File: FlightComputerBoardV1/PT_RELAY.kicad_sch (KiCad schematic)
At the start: 4 parts, among them J1 Screw_Terminal_01x02, J2 Screw_Terminal_01x02, J3 Screw_Terminal_01x02, J4 Screw_Terminal_01x02

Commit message: Added PTs
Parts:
- added C1, C2, C3, C4, C5, C6: 0.1u, symbol Device:C
- added J5: PT5, symbol Connector:Screw_Terminal_01x02
- added J6: PT6, symbol Connector:Screw_Terminal_01x02
- added R1, R11, R3, R5, R7, R9: 1k, symbol Device:R_US
- added R10, R12, R2, R4, R6, R8: 160, symbol Device:R_US
- J1: value Screw_Terminal_01x02 -> PT1
- J2: value Screw_Terminal_01x02 -> PT2
- J3: value Screw_Terminal_01x02 -> PT3
- J4: value Screw_Terminal_01x02 -> PT4
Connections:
- net +24V: now reaches J3.1 (Pin_1)
- net +24V: now also J1.1 (Pin_1), J2.1 (Pin_1), J4.1 (Pin_1), J5.1 (Pin_1), J6.1 (Pin_1)
- net at J3.2 (Pin_2): now also R5.1
- net at J4.2 (Pin_2): now also R7.1
- net at J1.2 (Pin_2): now also R1.1
- net at J2.2 (Pin_2): now also R3.1
- new net: J5.2 (Pin_2), R9.1
- new net: J6.2 (Pin_2), R11.1
- new net GND: C1.2, C2.2, C3.2, C4.2, C5.2, C6.2, R10.2, R12.2, R2.2, R4.2, R6.2, R8.2
- new net PT1: C1.1, R1.2, R2.1
- new net PT2: C2.1, R3.2, R4.1
- new net PT3: C3.1, R5.2, R6.1
- new net PT4: C4.1, R7.2, R8.1
- new net PT5: C5.1, R10.1, R9.2
- new net PT6: C6.1, R11.2, R12.1
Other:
- moved on the sheet: J1

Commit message: Added 9 PTs circuit
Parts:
- added C7, C8, C9: 0.1u, symbol Device:C
- added J7: PT7, symbol Connector:Screw_Terminal_01x02
- added J8: PT8, symbol Connector:Screw_Terminal_01x02
- added J9: PT9, symbol Connector:Screw_Terminal_01x02
- added R13, R15, R17: 1k, symbol Device:R_US
- added R14, R16, R18: 160, symbol Device:R_US
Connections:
- net +24V: now also J7.1 (Pin_1), J8.1 (Pin_1), J9.1 (Pin_1)
- net GND: now also C7.2, C8.2, C9.2, R14.2, R16.2, R18.2
- new net: J9.2 (Pin_2), R17.1
- new net: J7.2 (Pin_2), R13.1
- new net: J8.2 (Pin_2), R15.1
- new net PT7: C7.1, R13.2, R14.1
- new net PT8: C8.1, R15.2, R16.1
- new net PT9: C9.1, R17.2, R18.1
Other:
- note added: "9x PRESSURE TRANSDUCERS"
- moved on the sheet: C1, C2, C3, C4, C5, C6, J1, J2, J3, J4, J5, J6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

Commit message: Added 6x relay-driven solenoids circuit
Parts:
- added D1, D2, D3, D4, D5, D6: 1N4007, Diode_THT:D_DO-41_SOD81_P10.16mm_Horizontal, symbol Diode:1N4007
- added J10: RELAY1, symbol Connector:Screw_Terminal_01x02
- added J11: RELAY4, symbol Connector:Screw_Terminal_01x02
- added J12: RELAY2, symbol Connector:Screw_Terminal_01x02
- added J13: RELAY5, symbol Connector:Screw_Terminal_01x02
- added J14: RELAY3, symbol Connector:Screw_Terminal_01x02
- added J15: RELAY6, symbol Connector:Screw_Terminal_01x02
- added Q1, Q2, Q3, Q4, Q5, Q6: Q_NPN, symbol Device:Q_NPN
- added R19, R24, R29, R30, R37, R38: 670, symbol Device:R_US
- added R20, R22, R23, R26, R27, R28, R33, R34, R35, R36, R41, R42: 10k, symbol Device:R_US
- added R21, R25, R31, R32, R39, R40: 4.7k, symbol Device:R_US
- added U1, U2, U3, U4, U5, U6: PS2811-1-F3-A, PS2811-1_REN, symbol PS2811_1_F3_A:PS2811-1-F3-A
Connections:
- net GND: now also R20.1, R23.1, R27.1, R28.1, R35.1, R36.1, U1.2 (CATHODE), U2.2 (CATHODE), U3.2 (CATHODE), U4.2 (CATHODE), U5.2 (CATHODE), U6.2 (CATHODE)
- new net: D1.2 (A), J10.2 (Pin_2), Q1.C
- new net: Q5.B, R39.2, R41.2
- new net: D5.2 (A), J14.2 (Pin_2), Q5.C
- new net: R31.1, U3.3 (EMITTER)
- new net: Q3.B, R31.2, R33.2
- new net: Q6.B, R40.2, R42.2
- new net: D4.2 (A), J13.2 (Pin_2), Q4.C
- new net: R38.2, U6.1 (ANODE)
- new net: R40.1, U6.3 (EMITTER)
- new net: Q4.B, R32.2, R34.2
- new net: D6.2 (A), J15.2 (Pin_2), Q6.C
- new net: R37.2, U5.1 (ANODE)
- new net: R24.2, U2.1 (ANODE)
- new net: R25.1, U2.3 (EMITTER)
- new net: Q1.B, R21.2, R22.2
- new net: R21.1, U1.3 (EMITTER)
- new net: D3.2 (A), J12.2 (Pin_2), Q3.C
- new net: R30.2, U4.1 (ANODE)
- new net: R39.1, U5.3 (EMITTER)
- new net: Q2.B, R25.2, R26.2
- new net: D2.2 (A), J11.2 (Pin_2), Q2.C
- new net: R19.2, U1.1 (ANODE)
- new net: R29.2, U3.1 (ANODE)
- new net: R32.1, U4.3 (EMITTER)
- new net HI_24V: D1.1 (K), D2.1 (K), D3.1 (K), D4.1 (K), D5.1 (K), D6.1 (K), J10.1 (Pin_1), J11.1 (Pin_1), J12.1 (Pin_1), J13.1 (Pin_1), J14.1 (Pin_1), J15.1 (Pin_1), U1.4 (COLLECTOR), U2.4 (COLLECTOR), U3.4 (COLLECTOR), U4.4 (COLLECTOR), U5.4 (COLLECTOR), U6.4 (COLLECTOR)
- new net HI_24_GND: Q1.E, Q2.E, Q3.E, Q4.E, Q5.E, Q6.E, R22.1, R26.1, R33.1, R34.1, R41.1, R42.1
- new net RELAY1: R19.1, R20.2
- new net RELAY2: R27.2, R29.1
- new net RELAY3: R35.2, R37.1
- new net RELAY4: R23.2, R24.1
- new net RELAY5: R28.2, R30.1
- new net RELAY6: R36.2, R38.1
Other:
- note added: "6x RELAY-DRIVEN SOLENOIDS"

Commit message: Added sheets and hierarchy labels
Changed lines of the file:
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@@
 		)
 	)
-	(global_label "PT7"
+	(hierarchical_label "PT3"
 		(shape output)
-		(at 281.94 50.8 180)
-		(fields_autoplaced yes)
+		(at 123.19 50.8 180)
 		(effects
 			(font
@@
 			(justify right)
 		)
-		(property "Intersheetrefs" "${INTERSHEET_REFS}"
-			(at 275.5077 50.8 0)
-			(hide yes)
-			(show_name no)
-			(do_not_autoplace no)
-			(effects
-				(font
-					(size 1.27 1.27)
-				)
-				(justify right)
-			)
-		)
 	)
-	(global_label "PT2"
+	(hierarchical_label "PT2"
 		(shape output)
 		(at 80.01 50.8 180)
-		(fields_autoplaced yes)
 		(effects
 			(font
@@
 			(justify right)
 		)
-		(property "Intersheetrefs" "${INTERSHEET_REFS}"
-			(at 73.5777 50.8 0)
-			(hide yes)
-			(show_name no)
-			(do_not_autoplace no)
-			(effects
-				(font
-					(size 1.27 1.27)
-				)
-				(justify right)
-			)
-		)
 	)
-	(global_label "PT1"
+	(hierarchical_label "PT6"
 		(shape output)
-		(at 36.83 50.8 180)
-		(fields_autoplaced yes)
+		(at 246.38 50.8 180)
 		(effects
 			(font
@@
 			(justify right)
 		)
-		(property "Intersheetrefs" "${INTERSHEET_REFS}"
-			(at 30.3977 50.8 0)
-			(hide yes)
-			(show_name no)
-			(do_not_autoplace no)
-			(effects
-				(font
-					(size 1.27 1.27)
-				)
-				(justify right)
-			)
-		)
 	)
-	(global_label "PT9"
+	(hierarchical_label "PT5"
 		(shape output)
-		(at 365.76 50.8 180)
-		(fields_autoplaced yes)
+		(at 208.28 50.8 180)
 		(effects
 			(font
@@
 			(justify right)
 		)
-		(property "Intersheetrefs" "${INTERSHEET_REFS}"
-			(at 359.3277 50.8 0)
-			(hide yes)
-			(show_name no)
-			(do_not_autoplace no)
-			(effects
-				(font
-					(size 1.27 1.27)
-				)
-				(justify right)
-			)
-		)
 	)
-	(global_label "PT8"
+	(hierarchical_label "PT1"
 		(shape output)
-		(at 322.58 50.8 180)
-		(fields_autoplaced yes)
+		(at 36.83 50.8 180)
 		(effects
 			(font
@@
 			(justify right)
 		)
-		(property "Intersheetrefs" "${INTERSHEET_REFS}"
-			(at 316.1477 50.8 0)
-			(hide yes)
-			(show_name no)
-			(do_not_autoplace no)
-			(effects
-				(font
-					(size 1.27 1.27)
-				)
-				(justify right)
-			)
-		)
 	)
-	(global_label "PT4"
+	(hierarchical_label "PT4"
 		(shape output)
 		(at 166.37 50.8 180)
-		(fields_autoplaced yes)
 		(effects
 			(font
@@
 			(justify right)
 		)
-		(property "Intersheetrefs" "${INTERSHEET_REFS}"
-			(at 159.9377 50.8 0)
-			(hide yes)
-			(show_name no)
-			(do_not_autoplace no)
-			(effects
-				(font
-					(size 1.27 1.27)
-				)
-				(justify right)
-			)
-		)
 	)
-	(global_label "PT5"
+	(hierarchical_label "PT7"
 		(shape output)
-		(at 208.28 50.8 180)
-		(fields_autoplaced yes)
+		(at 281.94 50.8 180)
 		(effects
 			(font
@@
 			(justify right)
 		)
-		(property "Intersheetrefs" "${INTERSHEET_REFS}"
-			(at 201.8477 50.8 0)
-			(hide yes)
-			(show_name no)
-			(do_not_autoplace no)
-			(effects
-				(font
-					(size 1.27 1.27)
-				)
-				(justify right)
-			)
-		)
 	)
-	(global_label "PT3"
+	(hierarchical_label "PT8"
 		(shape output)
-		(at 123.19 50.8 180)
-		(fields_autoplaced yes)
+		(at 322.58 50.8 180)
 		(effects
 			(font
@@
 			(justify right)
 		)
-		(property "Intersheetrefs" "${INTERSHEET_REFS}"
-			(at 116.7577 50.8 0)
-			(hide yes)
-			(show_name no)
-			(do_not_autoplace no)
-			(effects
-				(font
-					(size 1.27 1.27)
-				)
-				(justify right)
-			)
-		)
 	)
-	(global_label "PT6"
+	(hierarchical_label "PT9"
 		(shape output)
-		(at 246.38 50.8 180)
-		(fields_autoplaced yes)
+		(at 365.76 50.8 180)
 		(effects
 			(font
@@
 			(justify right)
 		)
-		(property "Intersheetrefs" "${INTERSHEET_REFS}"
-			(at 239.9477 50.8 0)
-			(hide yes)
-			(show_name no)
-			(do_not_autoplace no)
-			(effects
-				(font
-					(size 1.27 1.27)
-				)
-				(justify right)
-			)
-		)
 	)

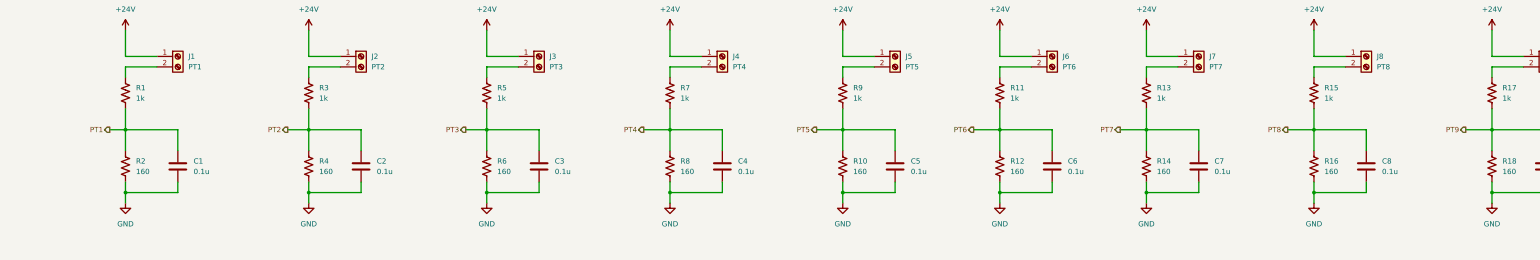
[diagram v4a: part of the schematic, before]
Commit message: Addition to MCU sheet and peripheral connection complete
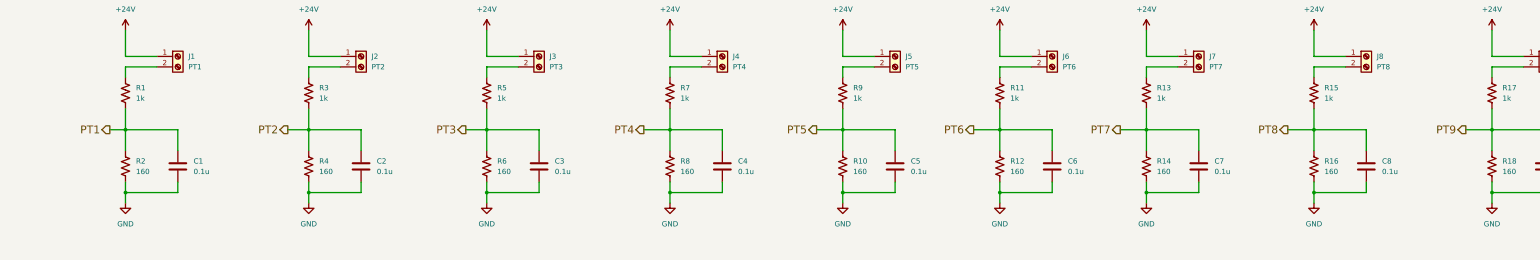
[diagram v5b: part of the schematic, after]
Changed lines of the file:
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@@
 		(effects
 			(font
-				(size 1.27 1.27)
+				(size 1.905 1.905)
 			)
 			(justify right)
@@
 		(effects
 			(font
-				(size 1.27 1.27)
+				(size 1.905 1.905)
 			)
 			(justify right)
@@
 		(effects
 			(font
-				(size 1.27 1.27)
+				(size 1.905 1.905)
 			)
 			(justify right)
@@
 		(effects
 			(font
-				(size 1.27 1.27)
+				(size 1.905 1.905)
 			)
 			(justify right)
@@
 		(effects
 			(font
-				(size 1.27 1.27)
+				(size 1.905 1.905)
 			)
 			(justify right)
@@
 		(effects
 			(font
-				(size 1.27 1.27)
+				(size 1.905 1.905)
 			)
 			(justify right)
@@
 		(effects
 			(font
-				(size 1.27 1.27)
+				(size 1.905 1.905)
 			)
 			(justify right)
@@
 		(effects
 			(font
-				(size 1.27 1.27)
+				(size 1.905 1.905)
 			)
 			(justify right)
@@
 		(effects
 			(font
-				(size 1.27 1.27)
+				(size 1.905 1.905)
 			)
 			(justify right)

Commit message: Late night shenanigans
- Added radar module sheet
- Created symbols for: radar, RFD900xus
- Added RFD900xus
- Fixed PT voltage dividers
To do:
- Add decoupling and test points
- Finish finding appropriate gate driver for H bridge linear actuator circuit
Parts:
- removed R1: 1k, symbol Device:R_US
- added R118: 1k, symbol Device:R_US
- R10, R12, R14, R16, R18, R2, R4, R6, R8: value 160 -> 1k
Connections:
- net PT1: now also R118.1; no longer C1.1, R2.1
- net PT2: now also R3.1; no longer C2.1, R3.2, R4.1
- net PT3: now also R5.1; no longer C3.1, R5.2, R6.1
- net PT4: now also R7.1; no longer C4.1, R7.2, R8.1
- net PT5: now also R9.1; no longer C5.1, R10.1, R9.2
- net PT6: now also R11.1; no longer C6.1, R11.2, R12.1
- net PT7: now also R13.1; no longer C7.1, R13.2, R14.1
- net PT8: now also R15.1; no longer C8.1, R15.2, R16.1
- net PT9: now also R17.1; no longer C9.1, R17.2, R18.1
- net at J9.2 (Pin_2): now also C9.1, R17.2, R18.1; no longer R17.1
- net at J5.2 (Pin_2): now also C5.1, R10.1, R9.2; no longer R9.1
- net at J6.2 (Pin_2): now also C6.1, R11.2, R12.1; no longer R11.1
- net at J7.2 (Pin_2): now also C7.1, R13.2, R14.1; no longer R13.1
- net at J8.2 (Pin_2): now also C8.1, R15.2, R16.1; no longer R15.1
- net at J2.2 (Pin_2): now also C2.1, R3.2, R4.1; no longer R3.1
- net at J4.2 (Pin_2): now also C4.1, R7.2, R8.1; no longer R7.1
- net at J3.2 (Pin_2): now also C3.1, R5.2, R6.1; no longer R5.1
- net at J1.2 (Pin_2): now also C1.1, R2.1, R118.2
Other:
- note added: "Most likely don't need diodes since series 1k should lower voltage enough."
- moved on the sheet: C1, C2, C3, C4, C5, C6, C7, C8, C9, J1, J2, J3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

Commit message: The Calamity
Design Changes:
- Swapped actuators to run on H bridge circuit
- Added potentiometer feedback for actuators
- Assigned pins for actuator control
- Added gate driver circuits
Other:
- Created very preliminary BOM (lifesucks.csv)
- Assigned most footprints

To do:
- Standardize component naming
- Finalize BOM (screw terminals once physical design starts)
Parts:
- C1, C2, C3, C4, C5, C6, C7, C8, C9: footprint (none) -> FlightComputerBoardV1_Footprints:CAP_GCM15_MUR
- R10, R11, R12, R13, R14, R15, R16, R17, R18, R2, R3, R4, R5, R6, R7, R8, R9: footprint (none) -> FlightComputerBoardV1_Footprints:RES_CRCW_0805
- R20, R22, R23, R26, R27, R28, R33, R34, R35, R36, R41, R42: footprint (none) -> FlightComputerBoardV1_Footprints:RC0805N_YAG
- R21, R25, R31, R32, R39, R40: footprint (none) -> FlightComputerBoardV1_Footprints:RES_RC0805_YAG
- U1, U2, U3, U4, U5, U6: footprint PS2811-1_REN -> FlightComputerBoardV1_Footprints:PS2811-1_REN
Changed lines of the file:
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@@
 			)
 		)
-		(property "Footprint" ""
+		(property "Footprint" "FlightComputerBoardV1_Footprints:RC0805N_YAG"
 			(at 34.544 221.996 90)
 			(hide yes)
@@
 			)
 		)
-		(property "Footprint" ""
+		(property "Footprint" "FlightComputerBoardV1_Footprints:RES_CRCW_0805"
 			(at 124.206 52.324 90)
 			(hide yes)
@@
 			)
 		)
-		(property "Footprint" ""
+		(property "Footprint" "FlightComputerBoardV1_Footprints:RC0805N_YAG"
 			(at 292.354 220.726 90)
 			(hide yes)
@@
 			)
 		)
-		(property "Footprint" ""
+		(property "Footprint" "FlightComputerBoardV1_Footprints:RES_RC0805_YAG"
 			(at 241.554 164.084 90)
 			(hide yes)
@@
 			)
 		)
-		(property "Footprint" ""
+		(property "Footprint" "FlightComputerBoardV1_Footprints:RES_CRCW_0805"
 			(at 167.386 52.324 90)
 			(hide yes)
@@
 			)
 		)
-		(property "Footprint" ""
+		(property "Footprint" "FlightComputerBoardV1_Footprints:RES_CRCW_0805"
 			(at 373.634 42.164 90)
 			(hide yes)
@@
 			)
 		)
-		(property "Footprint" ""
+		(property "Footprint" "FlightComputerBoardV1_Footprints:RES_CRCW_0805"
 			(at 71.374 42.164 90)
 			(hide yes)
@@
 			)
 		)
-		(property "Footprint" ""
+		(property "Footprint" "FlightComputerBoardV1_Footprints:RC0805N_YAG"
 			(at 374.904 224.536 90)
 			(hide yes)
@@
 			)
 		)
-		(property "Footprint" ""
+		(property "Footprint" "FlightComputerBoardV1_Footprints:CAP_GCM15_MUR"
 			(at 395.9352 55.88 0)
 			(hide yes)
@@
 			)
 		)
-		(property "Footprint" "PS2811-1_REN"
+		(property "Footprint" "FlightComputerBoardV1_Footprints:PS2811-1_REN"
 			(at 309.88 215.9 0)
 			(hide yes)
@@
 			)
 		)
-		(property "Footprint" ""
+		(property "Footprint" "FlightComputerBoardV1_Footprints:RES_CRCW_0805"
 			(at 244.094 42.164 90)
 			(hide yes)
@@
 			)
 		)
-		(property "Footprint" ""
+		(property "Footprint" "FlightComputerBoardV1_Footprints:RC0805N_YAG"
 			(at 245.364 225.806 90)
 			(hide yes)
@@
 			)
 		)
-		(property "Footprint" ""
+		(property "Footprint" "FlightComputerBoardV1_Footprints:RES_CRCW_0805"
 			(at 253.746 52.324 90)
 			(hide yes)
@@
 			)
 		)
-		(property "Footprint" ""
+		(property "Footprint" "FlightComputerBoardV1_Footprints:CAP_GCM15_MUR"
 			(at 352.7552 55.88 0)
 			(hide yes)
@@
 			)
 		)
-		(property "Footprint" ""
+		(property "Footprint" "FlightComputerBoardV1_Footprints:CAP_GCM15_MUR"
 			(at 309.5752 55.88 0)
 			(hide yes)
@@
 			)
 		)
-		(property "Footprint" ""
+		(property "Footprint" "FlightComputerBoardV1_Footprints:RES_CRCW_0805"
 			(at 340.106 52.324 90)
 			(hide yes)
@@
 			)
 		)
-		(property "Footprint" "PS2811-1_REN"
+		(property "Footprint" "FlightComputerBoardV1_Footprints:PS2811-1_REN"
 			(at 52.07 217.17 0)
 			(hide yes)
@@
 			)
 		)
-		(property "Footprint" ""
+		(property "Footprint" "FlightComputerBoardV1_Footprints:RC0805N_YAG"
 			(at 117.094 171.196 90)
 			(hide yes)
@@
 			)
 		)
-		(property "Footprint" ""
+		(property "Footprint" "FlightComputerBoardV1_Footprints:RES_CRCW_0805"
 			(at 210.566 52.324 90)
 			(hide yes)
@@
 			)
 		)
-		(property "Footprint" ""
+		(property "Footprint" "FlightComputerBoardV1_Footprints:RES_CRCW_0805"
 			(at 81.026 52.324 90)
 			(hide yes)
@@
 			)
 		)
-		(property "Footprint" ""
+		(property "Footprint" "FlightComputerBoardV1_Footprints:RES_CRCW_0805"
 			(at 287.274 42.164 90)
 			(hide yes)
@@
 			)
 		)
-		(property "Footprint" ""
+		(property "Footprint" "FlightComputerBoardV1_Footprints:RES_CRCW_0805"
 			(at 330.454 42.164 90)
 			(hide yes)
@@
 			)
 		)
-		(property "Footprint" ""
+		(property "Footprint" "FlightComputerBoardV1_Footprints:RES_CRCW_0805"
 			(at 157.734 42.164 90)
 			(hide yes)
@@
 			)
 		)
-		(property "Footprint" ""
+		(property "Footprint" "FlightComputerBoardV1_Footprints:RES_RC0805_YAG"
 			(at 113.284 164.084 90)
 			(hide yes)
@@
 			)
 		)
-		(property "Footprint" ""
+		(property "Footprint" "FlightComputerBoardV1_Footprints:RES_CRCW_0805"
 			(at 383.286 52.324 90)
 			(hide yes)
@@
 			)
 		)
-		(property "Footprint" ""
+		(property "Footprint" "FlightComputerBoardV1_Footprints:RC0805N_YAG"
 			(at 162.814 221.996 90)
 			(hide yes)
@@
 			)
 		)
-		(property "Footprint" ""
+		(property "Footprint" "FlightComputerBoardV1_Footprints:RC0805N_YAG"
 			(at 292.354 166.116 90)
 			(hide yes)
@@
 			)
 		)
-		(property "Footprint" ""
+		(property "Footprint" "FlightComputerBoardV1_Footprints:CAP_GCM15_MUR"
 			(at 136.8552 55.88 0)
 			(hide yes)
@@
 			)
 		)
-		(property "Footprint" "PS2811-1_REN"
+		(property "Footprint" "FlightComputerBoardV1_Footprints:PS2811-1_REN"
 			(at 309.88 161.29 0)
 			(hide yes)
@@
 			)
 		)
-		(property "Footprint" ""
+		(property "Footprint" "FlightComputerBoardV1_Footprints:RES_RC0805_YAG"
 			(at 113.284 218.694 90)
 			(hide yes)
@@
 			)
 		)
-		(property "Footprint" ""
+		(property "Footprint" "FlightComputerBoardV1_Footprints:RC0805N_YAG"
 			(at 117.094 225.806 90)
 			(hide yes)
@@
 			)
 		)
-		(property "Footprint" ""
+		(property "Footprint" "FlightComputerBoardV1_Footprints:RES_CRCW_0805"
 			(at 296.926 52.324 90)
 			(hide yes)
@@
 			)
 		)
-		(property "Footprint" "PS2811-1_REN"
+		(property "Footprint" "FlightComputerBoardV1_Footprints:PS2811-1_REN"
 			(at 52.07 162.56 0)
 			(hide yes)
@@
 			)
 		)
-		(property "Footprint" ""
+		(property "Footprint" "FlightComputerBoardV1_Footprints:RC0805N_YAG"
 			(at 374.904 169.926 90)
 			(hide yes)
@@
 			)
 		)
-		(property "Footprint" ""
+		(property "Footprint" "FlightComputerBoardV1_Footprints:CAP_GCM15_MUR"
 			(at 93.6752 55.88 0)
 			(hide yes)
@@
 			)
 		)
-		(property "Footprint" ""
+		(property "Footprint" "FlightComputerBoardV1_Footprints:CAP_GCM15_MUR"
 			(at 223.2152 55.88 0)
 			(hide yes)
@@
 			)
 		)
-		(property "Footprint" ""
+		(property "Footprint" "FlightComputerBoardV1_Footprints:RES_CRCW_0805"
 			(at 200.914 42.164 90)
 			(hide yes)
@@
 			)
 		)
-		(property "Footprint" ""
+		(property "Footprint" "FlightComputerBoardV1_Footprints:RES_CRCW_0805"
 			(at 114.554 42.164 90)
 			(hide yes)
@@
 			)
 		)
-		(property "Footprint" ""
+		(property "Footprint" "FlightComputerBoardV1_Footprints:RC0805N_YAG"
 			(at 34.544 167.386 90)
 			(hide yes)
@@
 			)
 		)
-		(property "Footprint" ""
+		(property "Footprint" "FlightComputerBoardV1_Footprints:RES_CRCW_0805"
 			(at 37.846 52.324 90)
 			(hide yes)
@@
 			)
 		)
-		(property "Footprint" ""
+		(property "Footprint" "FlightComputerBoardV1_Footprints:RES_RC0805_YAG"
 			(at 371.094 162.814 90)
 			(hide yes)
@@
 			)
 		)
-		(property "Footprint" ""
+		(property "Footprint" "FlightComputerBoardV1_Footprints:CAP_GCM15_MUR"
 			(at 180.0352 55.88 0)
 			(hide yes)
@@
 			)
 		)
-		(property "Footprint" ""
+		(property "Footprint" "FlightComputerBoardV1_Footprints:RES_RC0805_YAG"
 			(at 241.554 218.694 90)
 			(hide yes)
@@
 			)
 		)
-		(property "Footprint" ""
+		(property "Footprint" "FlightComputerBoardV1_Footprints:CAP_GCM15_MUR"
 			(at 50.4952 55.88 0)
 			(hide yes)
@@
 			)
 		)
-		(property "Footprint" ""
+		(property "Footprint" "FlightComputerBoardV1_Footprints:CAP_GCM15_MUR"
 			(at 266.3952 55.88 0)
 			(hide yes)
@@
 			)
 		)
-		(property "Footprint" ""
+		(property "Footprint" "FlightComputerBoardV1_Footprints:RES_RC0805_YAG"
 			(at 371.094 217.424 90)
 			(hide yes)
@@
 			)
 		)
-		(property "Footprint" "PS2811-1_REN"
+		(property "Footprint" "FlightComputerBoardV1_Footprints:PS2811-1_REN"
 			(at 180.34 217.17 0)
 			(hide yes)
@@
 			)
 		)
-		(property "Footprint" ""
+		(property "Footprint" "FlightComputerBoardV1_Footprints:RC0805N_YAG"
 			(at 245.364 171.196 90)
 			(hide yes)
@@
 			)
 		)
-		(property "Footprint" "PS2811-1_REN"
+		(property "Footprint" "FlightComputerBoardV1_Footprints:PS2811-1_REN"
 			(at 180.34 162.56 0)
 			(hide yes)
@@
 			)
 		)
-		(property "Footprint" ""
+		(property "Footprint" "FlightComputerBoardV1_Footprints:RC0805N_YAG"
 			(at 162.814 167.386 90)
 			(hide yes)
